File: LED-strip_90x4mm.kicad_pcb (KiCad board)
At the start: 2 copper layers, 4 x 90 mm, 38 parts, among them P1 CONN_2, P10 CONN_2, P11 CONN_2, P12 CONN_2, P2 CONN_2, P3 CONN_2, P4 CONN_2, P5 CONN_2, P6 CONN_2, P7 CONN_2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

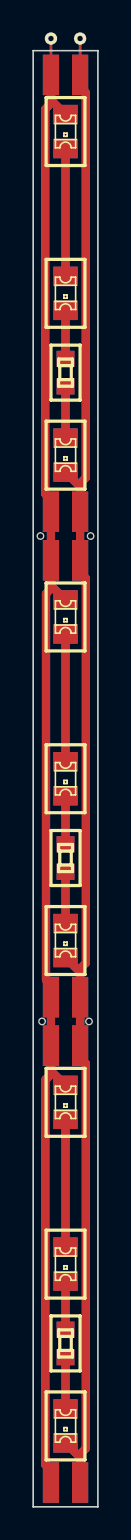
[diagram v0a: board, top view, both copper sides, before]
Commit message: Changed edge-connector footprint.
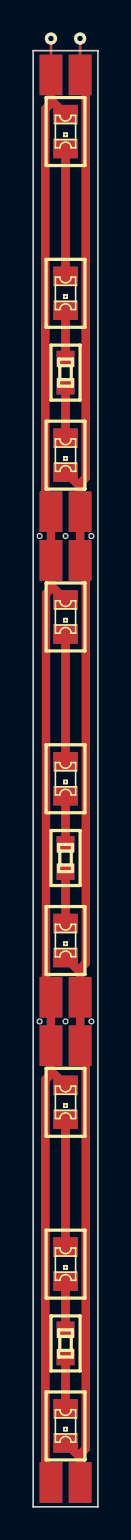
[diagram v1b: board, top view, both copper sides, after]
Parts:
- P1, P10, P11, P12, P2, P3, P4, P5, P6, P7, P8, P9: footprint my_parts:MADW__SIL-2 -> my_parts:MADW__SMD_2-pin_square_3.2x2.5mm
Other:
- board text added: "2014 V0.20.b"
- board text removed: "2014 V0.20.a"

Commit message: Some tweaks (single board for now). Panel later.
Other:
- board text added: "2014 V0.20.c"
- board text removed: "2014 V0.20.b"
